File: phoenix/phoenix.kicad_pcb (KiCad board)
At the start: 2 copper layers, 75 x 32 mm, 15 parts, among them J1 JST_B4B_XH_A, U1 Teensy4.1, U2 BMP280, U3 LIS3MDLTR, U4 LSM6DSOXTR

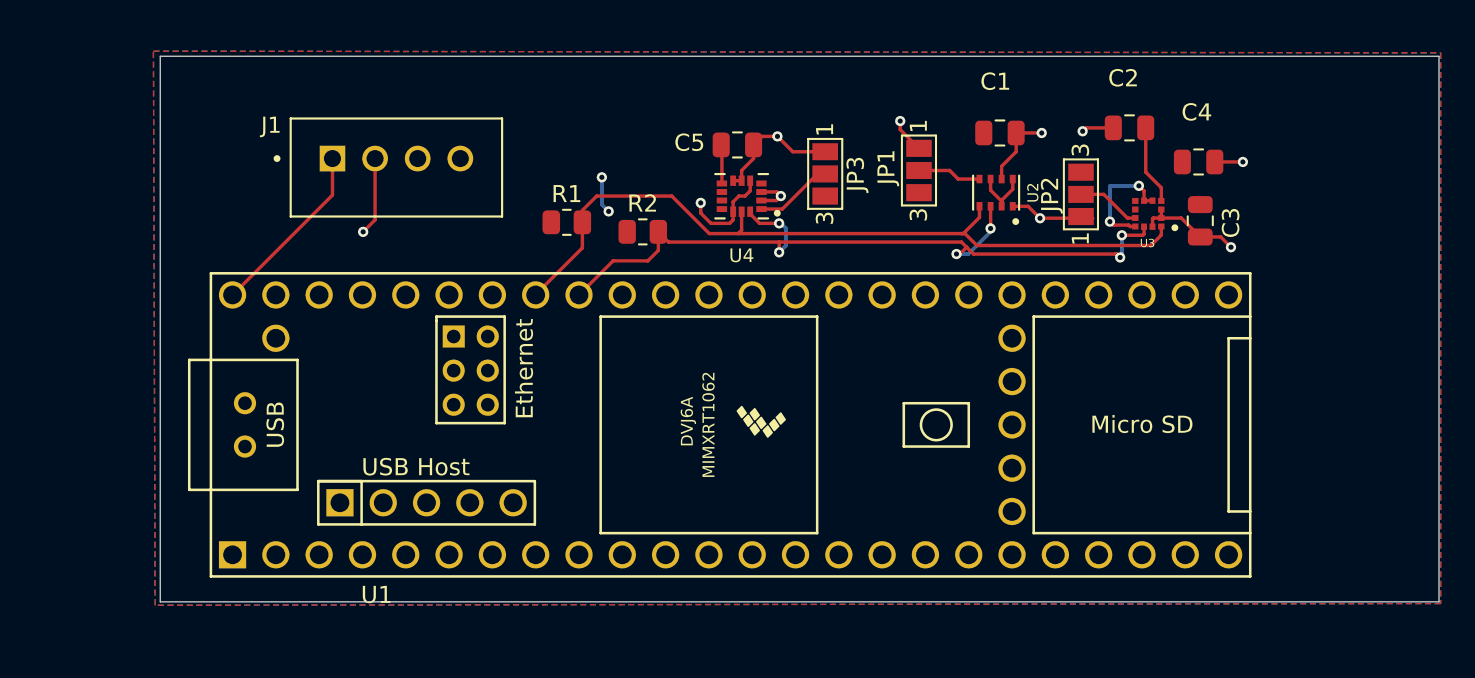
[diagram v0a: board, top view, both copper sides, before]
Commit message: Added backup radio and debug LEDs
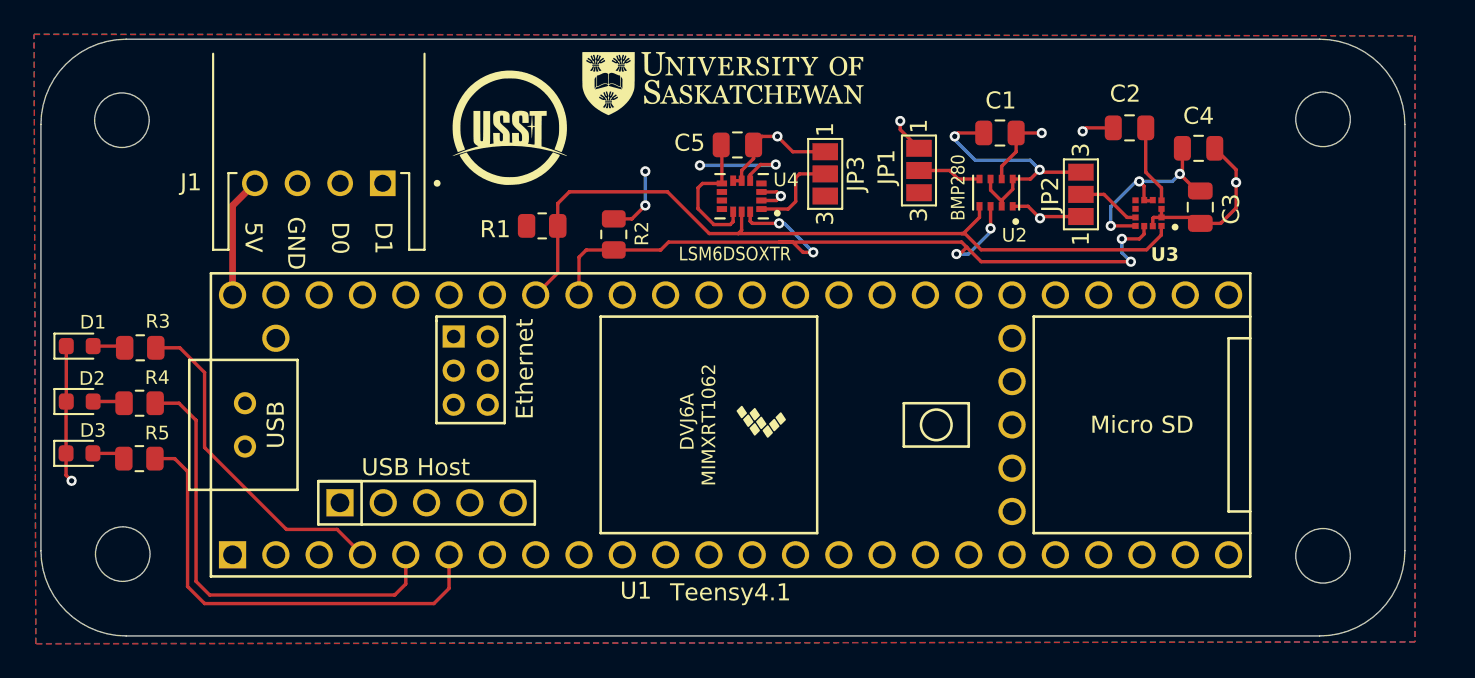
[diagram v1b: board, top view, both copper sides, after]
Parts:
- added D1: LED0, LED_SMD:LED_0603_1608Metric, F.Cu at (85.3, 67.6)
- added D2: LED1, LED_SMD:LED_0603_1608Metric, F.Cu at (85.3, 70.8)
- added D3: LED2, LED_SMD:LED_0603_1608Metric, F.Cu at (85.3, 73.9)
- added G***: LOGO, USST_logo:usask_logo_15x3.4_silkscreen, F.Cu at (123.0, 52.2)
- added G***: LOGO, USST_logo:USST_logo_Small, F.Cu at (110.5, 54.8)
- added H1: MountingHole, MountingHole:MountingHole_3.2mm_M3, F.Cu at (87.8, 54.4)
- added H2: MountingHole, MountingHole:MountingHole_3.2mm_M3, F.Cu at (87.8, 79.8)
- added H3: MountingHole, MountingHole:MountingHole_3.2mm_M3, F.Cu at (158.2, 54.3)
- added H4: MountingHole, MountingHole:MountingHole_3.2mm_M3, F.Cu at (158.2, 79.9)
- added R3: 10k, Resistor_SMD:R_0805_2012Metric, F.Cu at (88.8, 67.7)
- added R4: 10k, Resistor_SMD:R_0805_2012Metric, F.Cu at (88.8, 71.0)
- added R5: 10k, Resistor_SMD:R_0805_2012Metric, F.Cu at (88.8, 74.2)
- J1: value JST_B4B_XH_A -> JST_S4B-XH-A-1; footprint custom_library:JST_B4B-XH-A -> custom_library:JST_S4B-XH-A-1
- moved J1 4.64 mm to (99.3, 56.2)
- moved R2 1.71 mm to (116.6, 61.0), turned to -90 degrees
- moved R1 1.46 mm to (112.4, 60.5)
- moved C3 0.80 mm to (151.0, 59.5)
- moved C4 0.80 mm to (150.9, 56.0)
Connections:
- J1 pad 1: /5V_VIN -> unconnected-(J1-Pad1)
- J1 pad 2: GND -> unconnected-(J1-Pad2)
- J1 pad 3: unconnected-(J1-Pad3) -> GND
- J1 pad 4: unconnected-(J1-Pad4) -> /5V_VIN
- U1 pad 1: unconnected-(U1-GND-Pad1) -> GND
- U1 pad 4: unconnected-(U1-2_OUT2-Pad4) -> /LED0
- U1 pad 5: unconnected-(U1-3_LRCLK2-Pad5) -> /LED1
- U1 pad 6: unconnected-(U1-4_BCLK2-Pad6) -> /LED2
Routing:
- net /LED2: track 0.00 -> 27.1 mm
- net /LED1: track 0.00 -> 26.9 mm
- net VDD: track 20.8 -> 47.1 mm, vias 5 -> 9
- net /LED0: track 0.00 -> 19.7 mm
- net GND: track 36.2 -> 41.4 mm, vias 9 -> 8
- net /SDA: track 47.2 -> 50.9 mm
- net /5V_VIN: track 10.4 -> 7.09 mm
- net Net-(D3-A): track 0.00 -> 1.94 mm
- net Net-(D1-A): track 0.00 -> 1.89 mm
- net Net-(D2-A): track 0.00 -> 1.85 mm
- net /SCL: track 45.8 -> 47.3 mm
- net Net-(JP3-C): track 4.59 -> 5.41 mm
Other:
- board size 75 x 32 mm -> 80 x 35 mm
- board text added: "5V"
- board text added: "D0"
- board text added: "D1"
- board text added: "GND"

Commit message: Cutoff for LC2025
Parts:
- added G***: LOGO, custom_library:rocket_avionics_logo, F.Cu at (158.5, 63.8)
- added P**: LOGO, custom_library:phoenix_logo, F.Cu at (87.8, 60.6)
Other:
- board text added: "Not responsible for unplanned rapid disassembly."
- board text added: "Phoenix"

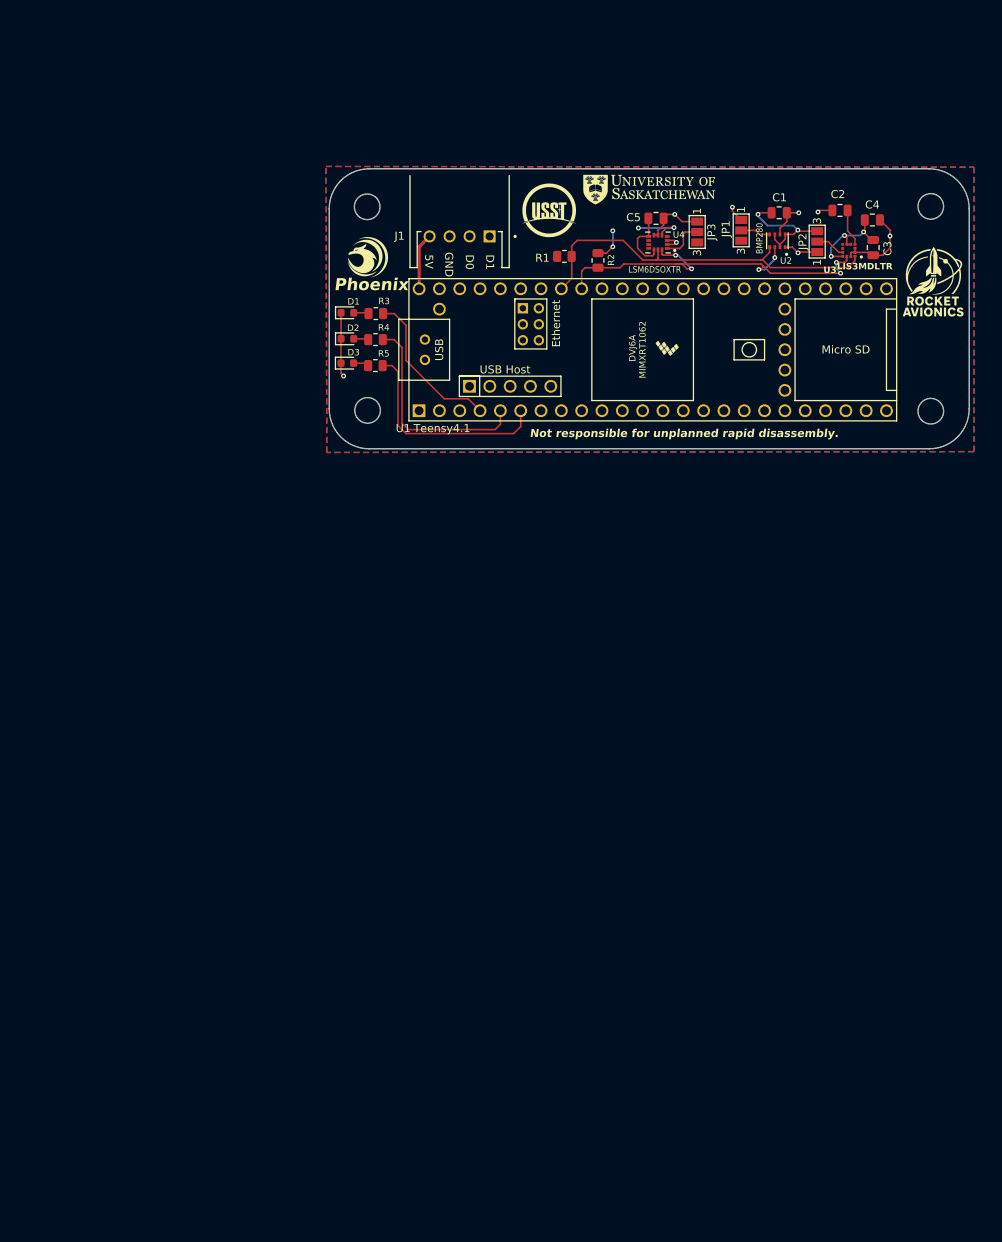
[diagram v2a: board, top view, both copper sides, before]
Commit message: Finished schematics and almost done layouts of LC26 PCBs
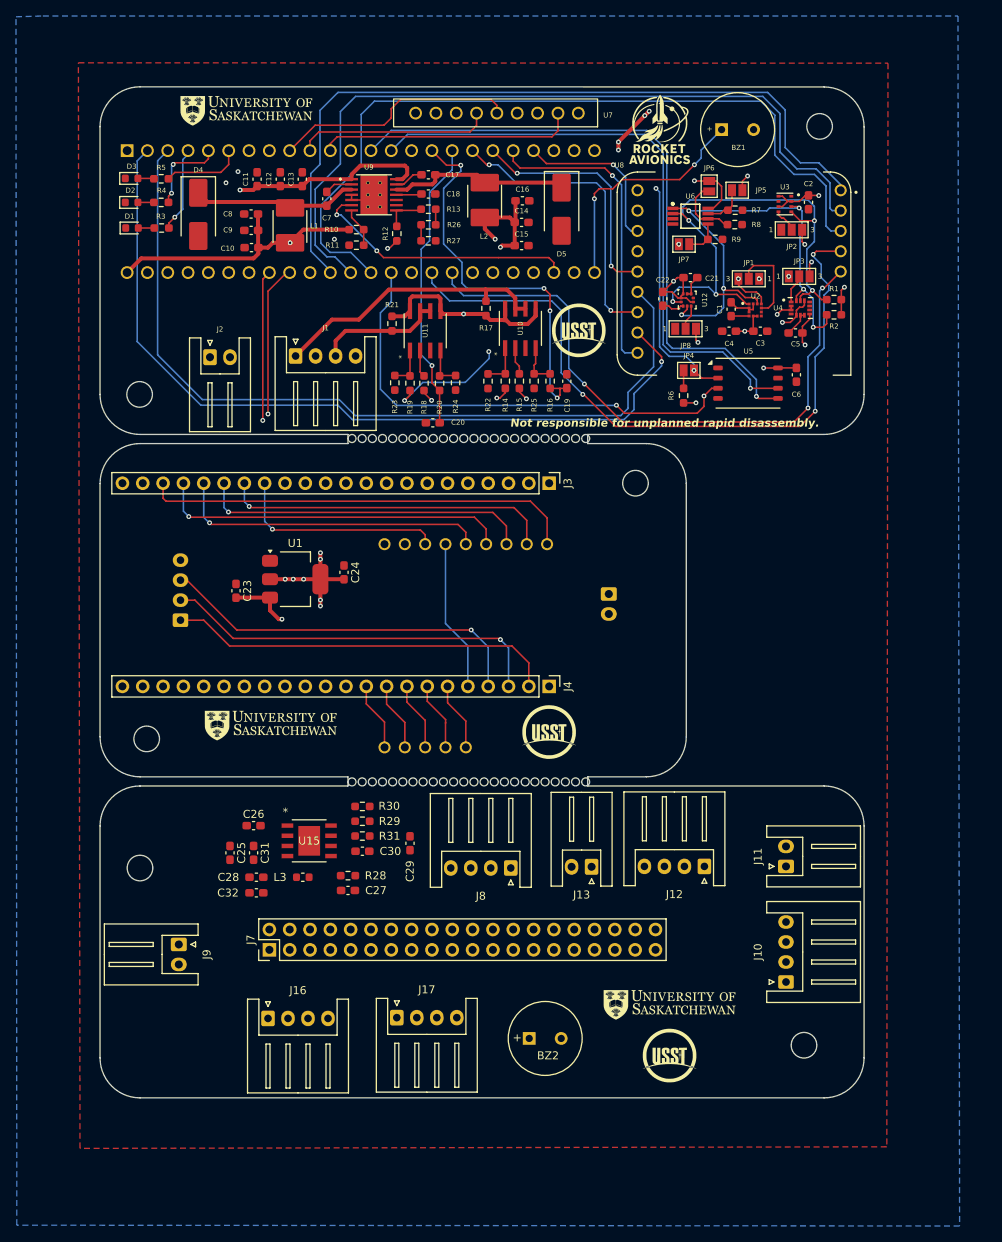
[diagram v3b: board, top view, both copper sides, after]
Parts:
- removed P**: LOGO, custom_library:phoenix_logo
- added BZ1: Buzzer, Buzzer_Beeper:MagneticBuzzer_PUI_AT-0927-TT-6-R, F.Cu at (132.1, 44.7)
- added BZ2: Buzzer, Buzzer_Beeper:MagneticBuzzer_PUI_AT-0927-TT-6-R, F.Cu at (108.0, 158.3)
- added C10: 10u, Capacitor_SMD:C_0603_1608Metric_Pad1.08x0.95mm_HandSolder, F.Cu at (73.3, 59.5)
- added C11: 100u, Capacitor_SMD:C_0603_1608Metric_Pad1.08x0.95mm_HandSolder, F.Cu at (74.0, 50.9)
- added C12: 10u, Capacitor_SMD:C_0603_1608Metric_Pad1.08x0.95mm_HandSolder, F.Cu at (76.9, 50.9)
- added C13: 10u, Capacitor_SMD:C_0603_1608Metric_Pad1.08x0.95mm_HandSolder, F.Cu at (79.6, 50.9)
- added C14: 10u, Capacitor_SMD:C_0603_1608Metric_Pad1.08x0.95mm_HandSolder, F.Cu at (107.0, 56.3)
- added C15: 10u, Capacitor_SMD:C_0603_1608Metric_Pad1.08x0.95mm_HandSolder, F.Cu at (107.0, 59.2)
- added C16: 100u, Capacitor_SMD:C_0603_1608Metric_Pad1.08x0.95mm_HandSolder, F.Cu at (107.2, 53.6)
- added C17: 22n, Capacitor_SMD:C_0603_1608Metric_Pad1.08x0.95mm_HandSolder, F.Cu at (95.4, 50.4)
- added C18: 10u, Capacitor_SMD:C_0603_1608Metric_Pad1.08x0.95mm_HandSolder, F.Cu at (95.4, 52.8)
- added C19: 100n, Capacitor_SMD:C_0603_1608Metric_Pad1.08x0.95mm_HandSolder, F.Cu at (112.7, 76.2)
- added C20: 100n, Capacitor_SMD:C_0603_1608Metric_Pad1.08x0.95mm_HandSolder, F.Cu at (96.0, 81.3)
- added C21: 100n, Capacitor_SMD:C_0603_1608Metric_Pad1.08x0.95mm_HandSolder, F.Cu at (128.2, 63.2)
- added C22: 100n, Capacitor_SMD:C_0603_1608Metric_Pad1.08x0.95mm_HandSolder, F.Cu at (124.7, 65.8)
- added C23: 100n, Capacitor_SMD:C_0603_1608Metric_Pad1.08x0.95mm_HandSolder, F.Cu at (71.3, 102.3)
- added C24: 10u, Capacitor_SMD:C_0603_1608Metric_Pad1.08x0.95mm_HandSolder, F.Cu at (84.8, 100.0)
- added C25: 22u, Capacitor_SMD:C_0603_1608Metric_Pad1.08x0.95mm_HandSolder, F.Cu at (70.6, 135.1)
- added C26: 47n, Capacitor_SMD:C_0603_1608Metric_Pad1.08x0.95mm_HandSolder, F.Cu at (73.5, 131.7)
- added C27: 100n, Capacitor_SMD:C_0603_1608Metric_Pad1.08x0.95mm_HandSolder, F.Cu at (85.3, 139.8)
- added C28: 47u, Capacitor_SMD:C_0603_1608Metric_Pad1.08x0.95mm_HandSolder, F.Cu at (73.9, 138.2)
- added C29: 3.3n, Capacitor_SMD:C_0603_1608Metric_Pad1.08x0.95mm_HandSolder, F.Cu at (93.1, 133.9)
- added C30: 1u, Capacitor_SMD:C_0603_1608Metric_Pad1.08x0.95mm_HandSolder, F.Cu at (87.2, 134.9)
- added C31: 22u, Capacitor_SMD:C_0603_1608Metric_Pad1.08x0.95mm_HandSolder, F.Cu at (73.5, 135.1)
- added C32: 47u, Capacitor_SMD:C_0603_1608Metric_Pad1.08x0.95mm_HandSolder, F.Cu at (73.9, 140.1)
- added C6: 100n, Capacitor_SMD:C_0603_1608Metric_Pad1.08x0.95mm_HandSolder, F.Cu at (141.4, 75.3)
- added C7: 22n, Capacitor_SMD:C_0603_1608Metric_Pad1.08x0.95mm_HandSolder, F.Cu at (82.7, 53.4)
- added C8: 100u, Capacitor_SMD:C_0603_1608Metric_Pad1.08x0.95mm_HandSolder, F.Cu at (73.2, 55.2)
- added C9: 10u, Capacitor_SMD:C_0603_1608Metric_Pad1.08x0.95mm_HandSolder, F.Cu at (73.2, 57.3)
- added D4: MBRS330T3, Diode_SMD:D_SMB_Handsoldering, F.Cu at (66.6, 55.3)
- added D5: MBRS330T3, Diode_SMD:D_SMB_Handsoldering, F.Cu at (112.0, 54.6)
- added G***: LOGO, USST_logo:usask_logo_15x3.4_silkscreen, F.Cu at (75.7, 119.2)
- added G***: LOGO, USST_logo:USST_logo_Small, F.Cu at (125.5, 160.5)
- added G***: LOGO, USST_logo:USST_logo_Small, F.Cu at (110.5, 120.0)
- added G***: LOGO, USST_logo:usask_logo_15x3.4_silkscreen, F.Cu at (125.5, 154.1)
- added H5: MountingHole, MountingHole:MountingHole_3.2mm_M3, F.Cu at (142.3, 159.2)
- added H6: MountingHole, MountingHole:MountingHole_3.2mm_M3, F.Cu at (59.4, 137.0)
- added J10: Conn_01x04_Pin, Connector_JST:JST_XH_S4B-XH-A_1x04_P2.50mm_Horizontal, F.Cu at (140.1, 151.2)
- added J11: Conn_01x02_Pin, Connector_JST:JST_XH_S2B-XH-A_1x02_P2.50mm_Horizontal, F.Cu at (140.1, 136.8)
- added J12: Conn_01x04_Pin, Connector_JST:JST_XH_S4B-XH-A_1x04_P2.50mm_Horizontal, F.Cu at (129.9, 136.8)
- added J13: Conn_01x02_Pin, Connector_JST:JST_XH_S2B-XH-A_1x02_P2.50mm_Horizontal, F.Cu at (115.8, 136.8)
- added J16: Conn_01x04_Pin, Connector_JST:JST_XH_S4B-XH-A_1x04_P2.50mm_Horizontal, F.Cu at (75.3, 155.8)
- added J17: Conn_01x04_Pin, Connector_JST:JST_XH_S4B-XH-A_1x04_P2.50mm_Horizontal, F.Cu at (91.5, 155.7)
- added J2: Conn_01x02_Pin, Connector_JST:JST_XH_S2B-XH-A_1x02_P2.50mm_Horizontal, F.Cu at (68.1, 73.2)
- added J3: Conn_01x22_Socket, Connector_PinHeader_2.54mm:PinHeader_1x22_P2.54mm_Vertical, F.Cu at (110.5, 88.9)
- added J4: Conn_01x22_Socket, Connector_PinHeader_2.54mm:PinHeader_1x22_P2.54mm_Vertical, F.Cu at (110.5, 114.3)
- added J5: Conn_01x04_Pin, Connector_JST:JST_XH_S4B-XH-A_1x04_P2.50mm_Horizontal, B.Cu at (64.4, 106.0)
- added J6: Conn_01x02_Pin, Connector_JST:JST_XH_S2B-XH-A_1x02_P2.50mm_Horizontal, B.Cu at (118.0, 102.8)
- added J7: Raspberry_Pi_4, Connector_PinHeader_2.54mm:PinHeader_2x20_P2.54mm_Vertical, F.Cu at (75.5, 147.2)
- added J8: Conn_01x04_Pin, Connector_JST:JST_XH_S4B-XH-A_1x04_P2.50mm_Horizontal, F.Cu at (105.7, 137.0)
- added J9: Conn_01x02_Pin, Connector_JST:JST_XH_S2B-XH-A_1x02_P2.50mm_Horizontal, F.Cu at (64.2, 146.6)
- added JP4: SD_nCS_Pull_Up, Jumper:SolderJumper-2_P1.3mm_Open_Pad1.0x1.5mm, F.Cu at (128.0, 74.8)
- added JP5: SolderJumper_2_Open, Jumper:SolderJumper-2_P1.3mm_Open_Pad1.0x1.5mm, F.Cu at (134.0, 52.3)
- added JP6: SolderJumper_2_Open, Jumper:SolderJumper-2_P1.3mm_Open_Pad1.0x1.5mm, F.Cu at (130.5, 51.8)
- added JP7: SolderJumper_2_Open, Jumper:SolderJumper-2_P1.3mm_Open_Pad1.0x1.5mm, F.Cu at (127.3, 59.0)
- added JP8: SolderJumper_3_Open, Jumper:SolderJumper-3_P1.3mm_Open_Pad1.0x1.5mm_NumberLabels, F.Cu at (127.5, 69.6)
- added L1: 22uH, custom_library:L_AMDLH5030S, F.Cu at (78.0, 56.8)
- added L2: 22uH, custom_library:L_AMDLH5030S, F.Cu at (102.3, 53.6)
- added L3: 4.7uH, Inductor_SMD:L_0603_1608Metric, F.Cu at (79.7, 138.2)
- added R10: 15k, Resistor_SMD:R_0603_1608Metric_Pad0.98x0.95mm_HandSolder, F.Cu at (86.4, 57.2)
- added R11: 2.7k, Resistor_SMD:R_0603_1608Metric_Pad0.98x0.95mm_HandSolder, F.Cu at (86.4, 59.1)
- added R12: 15k, Resistor_SMD:R_0603_1608Metric_Pad0.98x0.95mm_HandSolder, F.Cu at (91.5, 57.7)
- added R13: 2.7k, Resistor_SMD:R_0603_1608Metric_Pad0.98x0.95mm_HandSolder, F.Cu at (95.4, 54.6)
- added R14: 1k, Resistor_SMD:R_0603_1608Metric_Pad0.98x0.95mm_HandSolder, F.Cu at (105.0, 76.1)
- added R15: 15k, Resistor_SMD:R_0603_1608Metric_Pad0.98x0.95mm_HandSolder, F.Cu at (106.8, 76.1)
- added R16: 15k, Resistor_SMD:R_0603_1608Metric_Pad0.98x0.95mm_HandSolder, F.Cu at (110.6, 76.1)
- added R17: 15k, Resistor_SMD:R_0603_1608Metric_Pad0.98x0.95mm_HandSolder, F.Cu at (102.6, 67.0)
- added R18: 15k, Resistor_SMD:R_0603_1608Metric_Pad0.98x0.95mm_HandSolder, F.Cu at (94.8, 76.4)
- added R19: 1k, Resistor_SMD:R_0603_1608Metric_Pad0.98x0.95mm_HandSolder, F.Cu at (93.1, 76.4)
- added R20: 15k, Resistor_SMD:R_0603_1608Metric_Pad0.98x0.95mm_HandSolder, F.Cu at (96.8, 76.4)
- added R21: 15k, Resistor_SMD:R_0603_1608Metric_Pad0.98x0.95mm_HandSolder, F.Cu at (90.8, 69.0)
- added R22: 100k, Resistor_SMD:R_0603_1608Metric_Pad0.98x0.95mm_HandSolder, F.Cu at (102.8, 76.2)
- added R23: 100k, Resistor_SMD:R_0603_1608Metric_Pad0.98x0.95mm_HandSolder, F.Cu at (91.2, 76.3)
- added R24: 1k, Resistor_SMD:R_0603_1608Metric_Pad0.98x0.95mm_HandSolder, F.Cu at (98.8, 76.3)
- added R25: 1k, Resistor_SMD:R_0603_1608Metric_Pad0.98x0.95mm_HandSolder, F.Cu at (108.6, 76.1)
- added R26: 1k, Resistor_SMD:R_0603_1608Metric_Pad0.98x0.95mm_HandSolder, F.Cu at (95.4, 56.6)
- added R27: 1k, Resistor_SMD:R_0603_1608Metric_Pad0.98x0.95mm_HandSolder, F.Cu at (95.4, 58.6)
- added R28: 10, Resistor_SMD:R_0603_1608Metric_Pad0.98x0.95mm_HandSolder, F.Cu at (85.3, 138.0)
- added R29: 113k, Resistor_SMD:R_0603_1608Metric_Pad0.98x0.95mm_HandSolder, F.Cu at (87.2, 131.2)
- added R30: 15k, Resistor_SMD:R_0603_1608Metric_Pad0.98x0.95mm_HandSolder, F.Cu at (87.2, 129.3)
- added R31: 15k, Resistor_SMD:R_0603_1608Metric_Pad0.98x0.95mm_HandSolder, F.Cu at (87.2, 133.0)
- added R6: 15k, Resistor_SMD:R_0603_1608Metric_Pad0.98x0.95mm_HandSolder, F.Cu at (127.3, 78.0)
- added R7: 15k, Resistor_SMD:R_0603_1608Metric_Pad0.98x0.95mm_HandSolder, F.Cu at (133.8, 54.8)
- added R8: 15k, Resistor_SMD:R_0603_1608Metric_Pad0.98x0.95mm_HandSolder, F.Cu at (133.7, 56.6)
- added R9: 15k, Resistor_SMD:R_0603_1608Metric_Pad0.98x0.95mm_HandSolder, F.Cu at (131.2, 58.4)
- added REF**: mousebite, custom_library:mousebite, F.Cu at (101.1, 83.3)
- added REF**: mousebite, custom_library:mousebite, F.Cu at (107.5, 83.3)
- added REF**: mousebite, custom_library:mousebite, F.Cu at (89.7, 83.3)
- added REF**: mousebite, custom_library:mousebite, F.Cu at (97.3, 83.3)
- added REF**: mousebite, custom_library:mousebite, F.Cu at (93.5, 126.2)
- added REF**: mousebite, custom_library:mousebite, F.Cu at (99.8, 126.2)
- added REF**: mousebite, custom_library:mousebite, F.Cu at (98.6, 126.2)
- added REF**: mousebite, custom_library:mousebite, F.Cu at (102.4, 126.2)
- added REF**: mousebite, custom_library:mousebite, F.Cu at (115.1, 83.3)
- added REF**: mousebite, custom_library:mousebite, F.Cu at (90.9, 126.2)
- added REF**: mousebite, custom_library:mousebite, F.Cu at (113.8, 83.3)
- added REF**: mousebite, custom_library:mousebite, F.Cu at (90.9, 83.3)
- added REF**: mousebite, custom_library:mousebite, F.Cu at (97.3, 126.2)
- added REF**: mousebite, custom_library:mousebite, F.Cu at (112.5, 126.2)
- added REF**: mousebite, custom_library:mousebite, F.Cu at (88.4, 126.2)
- added REF**: mousebite, custom_library:mousebite, F.Cu at (101.1, 126.2)
- added REF**: mousebite, custom_library:mousebite, F.Cu at (96.0, 126.2)
- added REF**: mousebite, custom_library:mousebite, F.Cu at (106.2, 126.2)
- added REF**: mousebite, custom_library:mousebite, F.Cu at (104.9, 83.3)
- added REF**: mousebite, custom_library:mousebite, F.Cu at (92.2, 126.2)
- added REF**: mousebite, custom_library:mousebite, F.Cu at (108.7, 83.3)
- added REF**: mousebite, custom_library:mousebite, F.Cu at (87.1, 83.3)
- added REF**: mousebite, custom_library:mousebite, F.Cu at (102.4, 83.3)
- added REF**: mousebite, custom_library:mousebite, F.Cu at (103.6, 126.2)
- added REF**: mousebite, custom_library:mousebite, F.Cu at (111.3, 83.3)
- added REF**: mousebite, custom_library:mousebite, F.Cu at (94.7, 126.2)
- added REF**: mousebite, custom_library:mousebite, F.Cu at (98.6, 83.3)
- added REF**: mousebite, custom_library:mousebite, F.Cu at (88.4, 83.3)
- added REF**: mousebite, custom_library:mousebite, F.Cu at (106.2, 83.3)
- added REF**: mousebite, custom_library:mousebite, F.Cu at (93.5, 83.3)
- added REF**: mousebite, custom_library:mousebite, F.Cu at (115.1, 126.2)
- added REF**: mousebite, custom_library:mousebite, F.Cu at (85.9, 83.3)
- added REF**: mousebite, custom_library:mousebite, F.Cu at (103.6, 83.3)
- added REF**: mousebite, custom_library:mousebite, F.Cu at (112.5, 83.3)
- added REF**: mousebite, custom_library:mousebite, F.Cu at (107.5, 126.2)
- added REF**: mousebite, custom_library:mousebite, F.Cu at (110.0, 126.2)
- added REF**: mousebite, custom_library:mousebite, F.Cu at (111.3, 126.2)
- added REF**: mousebite, custom_library:mousebite, F.Cu at (104.9, 126.2)
- added REF**: mousebite, custom_library:mousebite, F.Cu at (113.8, 126.2)
- added REF**: mousebite, custom_library:mousebite, F.Cu at (89.7, 126.2)
- added REF**: mousebite, custom_library:mousebite, F.Cu at (108.7, 126.2)
- added REF**: mousebite, custom_library:mousebite, F.Cu at (96.0, 83.3)
- added REF**: mousebite, custom_library:mousebite, F.Cu at (99.8, 83.3)
- added REF**: mousebite, custom_library:mousebite, F.Cu at (85.9, 126.2)
- added REF**: mousebite, custom_library:mousebite, F.Cu at (110.0, 83.3)
- added REF**: mousebite, custom_library:mousebite, F.Cu at (87.1, 126.2)
- added REF**: mousebite, custom_library:mousebite, F.Cu at (92.2, 83.3)
- added REF**: mousebite, custom_library:mousebite, F.Cu at (94.7, 83.3)
- added U10: VN7140ASTR, custom_library:VN7140ASTR_SO-8, F.Cu at (106.9, 69.5)
- added U11: VN7140ASTR, custom_library:VN7140ASTR_SO-8, F.Cu at (95.0, 69.8)
- added U12: BMP581, Package_LGA:ST_HLGA-10_2x2mm_P0.5mm_LayoutBorder3x2y, F.Cu at (127.8, 66.0)
- added U13: Teensy4.1, custom_library:Teensy41_simplified, B.Cu at (87.0, 55.0)
- added U14: Adafruit_RFM9x, custom_library:Adafuit_RFM9x, B.Cu at (100.3, 108.6)
- added U15: AOZ6605PI-1, custom_library:SO8_EP1_AOS, F.Cu at (80.5, 133.6)
- added U5: XTSD04G, Package_LGA:LGA-8_8x6mm_P1.27mm, F.Cu at (135.3, 76.4)
- added U6: MCP9808T-E_MS, custom_library:MCP9808T-E_MS, F.Cu at (128.2, 55.5)
- added U7: Adafruit_Ult_GPS, custom_library:Adafruit_Ult_GPS, F.Cu at (116.5, 44.4)
- added U8: Adafruit_RFM9x, custom_library:Adafuit_RFM9x, F.Cu at (133.6, 62.7)
- added U9: TPS54386PWPR, custom_library:IC_TPS54386PWPR, F.Cu at (88.6, 52.9)
- C1: footprint Capacitor_SMD:C_0805_2012Metric -> Capacitor_SMD:C_0603_1608Metric_Pad1.08x0.95mm_HandSolder
- C2, C4, C5: value 100nF -> 100n; footprint Capacitor_SMD:C_0805_2012Metric -> Capacitor_SMD:C_0603_1608Metric_Pad1.08x0.95mm_HandSolder
- C3: value 1uF -> 1u; footprint Capacitor_SMD:C_0805_2012Metric -> Capacitor_SMD:C_0603_1608Metric_Pad1.08x0.95mm_HandSolder
- J1: value JST_S4B-XH-A-1 -> Conn_01x04_Pin; footprint custom_library:JST_S4B-XH-A-1 -> Connector_JST:JST_XH_S4B-XH-A_1x04_P2.50mm_Horizontal
- R1, R2, R3, R4, R5: footprint Resistor_SMD:R_0805_2012Metric -> Resistor_SMD:R_0603_1608Metric_Pad0.98x0.95mm_HandSolder
- U1: value Teensy4.1 -> LD1117S33TR_SOT223; footprint custom_library:Teensy41 -> Package_TO_SOT_SMD:SOT-223-3_TabPin2
- U2: value BMP280 -> LIS3MDLTR; footprint custom_library:BMP280 -> custom_library:LIS3MDLTR
- U3: value LIS3MDLTR -> BMP280; footprint custom_library:LIS3MDLTR -> custom_library:BMP280
- moved H4 98.9 mm to (59.3, 77.8), turned to -90 degrees
- moved H1 57.4 mm to (144.3, 44.3), turned to 90 degrees
- moved U1 53.1 mm to (78.8, 100.9)
- moved G*** 51.3 mm to (72.7, 42.4)
- moved H3 50.6 mm to (121.3, 88.9)
- moved H2 49.5 mm to (60.2, 120.9)
- moved G*** 39.1 mm to (124.3, 44.7)
- moved R5 35.5 mm to (62.0, 50.9)
- moved D3 35.5 mm to (58.3, 50.8)
- moved R1 34.1 mm to (146.1, 66.0), turned to 180 degrees
- moved D2 31.9 mm to (58.3, 53.8)
- moved R4 31.8 mm to (62.0, 53.8)
- moved R2 30.3 mm to (146.1, 67.8), turned to 180 degrees
- moved D1 28.9 mm to (58.4, 57.0)
- moved R3 28.8 mm to (62.0, 57.0)
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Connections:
- C1 pad 1: VDD -> Net-(U2-C1)
- C2 pad 1: Net-(U3-C1) -> +3V3
- C3 pad 1: VDD -> +3V3
- C4 pad 1: VDD -> +3V3
- C5 pad 2: VDD -> +3V3
- J1 pad 1: unconnected-(J1-Pad1) -> /Power/MAIN
- J1 pad 2: unconnected-(J1-Pad2) -> GND
- J1 pad 3: GND -> /Power/APOGEE
- J1 pad 4: /5V_VIN -> GND
- JP1 pad 3: VDD -> +3V3
- JP2 pad 3: VDD -> +3V3
- JP3 pad 3: VDD -> +3V3
- R1 pad 1: VDD -> +3V3
- R1 pad 2: /SCL -> I2C_SCL
- R2 pad 1: VDD -> +3V3
- R2 pad 2: /SDA -> I2C_SDA
- R3 pad 1: /LED0 -> /MCU/LED0
- R4 pad 1: /LED1 -> /MCU/LED1
- R5 pad 1: /LED2 -> /MCU/LED2
- U1 pad 2: unconnected-(U1-0_RX1_CRX2_CS1-Pad2) -> /interlink/VDD
- U1 pad 3: unconnected-(U1-1_TX1_CTX2_MISO1-Pad3) -> /interlink/VBAT
- U2 pad 1: GND -> I2C_SCL
- U2 pad 2: VDD -> GND
- U2 pad 3: /SDA -> GND
- U2 pad 4: /SCL -> Net-(U2-C1)
- U2 pad 5: Net-(JP1-C) -> +3V3
- U2 pad 6: VDD -> +3V3
- U2 pad 7: GND -> unconnected-(U2-INT-Pad7)
- U2 pad 8: VDD -> unconnected-(U2-DRDY-Pad8)
- U3 pad 1: /SCL -> GND
- U3 pad 2: GND -> +3V3
- U3 pad 3: GND -> I2C_SDA
- U3 pad 4: Net-(U3-C1) -> I2C_SCL
- U3 pad 5: VDD -> Net-(JP2-C)
- U3 pad 6: VDD -> +3V3
- U3 pad 7: /MAG_INT -> GND
- U3 pad 8: /MAG_DRDY -> +3V3
- U4 pad 12: VDD -> +3V3
- U4 pad 13: /SCL -> I2C_SCL
- U4 pad 14: /SDA -> I2C_SDA
- U4 pad 4: /IMU_INT1 -> unconnected-(U4-INT1-Pad4)
- U4 pad 5: VDD -> +3V3
- U4 pad 8: VDD -> +3V3
- U4 pad 9: /IMU_INT2 -> unconnected-(U4-INT2-Pad9)
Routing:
- net I2C_SCL: track 0.00 -> 173.1 mm, vias 0 -> 6
- net I2C_SDA: track 0.00 -> 168.0 mm, vias 0 -> 7
- net +VBAT: track 0.00 -> 126.3 mm, vias 0 -> 2
- net +5V: track 0.00 -> 115.4 mm, vias 0 -> 1
- net RADIO.MISO: track 0.00 -> 105.1 mm
- net RADIO.CS: track 0.00 -> 103.4 mm, vias 0 -> 1
- net RADIO.G3: track 0.00 -> 99.2 mm
- net RADIO.G2: track 0.00 -> 97.8 mm
- net RADIO.G1: track 0.00 -> 96.0 mm
- net RADIO.G4: track 0.00 -> 86.7 mm, vias 0 -> 3
- net +3V3: track 0.00 -> 86.7 mm, vias 0 -> 24
- net FLASH_SPI.nCS: track 0.00 -> 82.1 mm, vias 0 -> 2
- net FLASH_SPI.MOSI: track 0.00 -> 81.1 mm, vias 0 -> 1
- net RADIO.G5: track 0.00 -> 77.5 mm, vias 0 -> 3
- net FLASH_SPI.MISO: track 0.00 -> 77.0 mm, vias 0 -> 1
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- added copper zone on In2.Cu, net +3V3
- added copper zone on In2.Cu, net /interlink/VDD
- added copper zone on F.Cu, net GND
- added copper zone on In1.Cu, net GND
- removed copper zone on F.Cu, net VDD
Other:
- board size 80 x 35 mm -> 95.5 x 126.4 mm
- copper layers 2 -> 4
- board text removed: "5V"
- board text removed: "D0"
- board text removed: "D1"
- board text removed: "GND"
- board text removed: "Phoenix"
